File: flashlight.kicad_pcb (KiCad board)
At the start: 2 copper layers, 45 x 120 mm, 25 parts, among them J1 USB_B_Micro, J2 Conn_01x03_Pin, Q1 HSS2333, Q2 HSS2333, SW1 SW_DIP_x01, U1 LP4054HB5F, U2 MT3608

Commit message: copper pour
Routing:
- net Net-(U2-IN): track 41.4 -> 30.9 mm
- net Net-(D5-A): track 9.55 -> 0.00 mm
- net VOUT: track 20.0 -> 14.3 mm
- net Net-(D4-K): track 27.2 -> 28.2 mm
- added copper zone on B.Cu, net Net-(D5-A)
- added copper zone on B.Cu, net Net-(U2-IN)
- added copper zone on B.Cu, net VOUT

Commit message: v2.2.2
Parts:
- D2: value RED -> CHARGING
- D3: value GREEN -> CHARGED
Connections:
- net +5V renamed Net-(D1-A)
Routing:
- net GND: track 2.40 -> 0.00 mm
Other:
- board text added: "locked"

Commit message: tight sot23-6
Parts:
- removed R11: 10k, Resistor_SMD:R_0603_1608Metric
- U2: footprint Package_TO_SOT_SMD:SOT-23-6 -> SparkFun-Semiconductor-Standard:SOT23-6-Tight
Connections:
- C3 pad 1: Net-(U2-IN) -> Net-(U2-EN)
- L1 pad 1: Net-(U2-IN) -> Net-(U2-EN)
- SW1 pad 2: Net-(U2-IN) -> Net-(U2-EN)
- U2 pad 5: Net-(U2-IN) -> Net-(U2-EN)
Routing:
- net Net-(U2-IN): track 30.9 -> 0.00 mm
- net Net-(U2-EN): track 2.46 -> 30.9 mm
- added copper zone on B.Cu, net Net-(U2-EN)
- removed copper zone on B.Cu, net Net-(U2-IN)

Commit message: v2.3
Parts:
- moved C4 3.18 mm to (109.0, 134.1)
- moved U2 1.69 mm to (106.0, 132.9)
- moved D5 1.56 mm to (112.4, 133.2)
- moved R6 1.22 mm to (105.3, 136.1)
- moved R7 1.20 mm to (107.0, 136.1)
- moved C3 0.97 mm to (103.1, 132.8), turned to 90 degrees
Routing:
- net /Vf=0.6V: track 4.40 -> 2.33 mm
- net VOUT: track 14.3 -> 13.6 mm
- added copper zone on B.Cu, net /Vf=0.6V
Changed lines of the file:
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@@
   (net 19 "Net-(D3-K)")
   (footprint "Resistor_SMD:R_0603_1608Metric" (layer "B.Cu")
-    (at 107.9246 136.8896 -90)
+    (at 106.9848 136.144 -90)
     (descr "Resistor SMD 0603 (1608 Metric), square (rectangular) end terminal, IPC_7351 nominal, (Body size source: IPC-SM-782 page 72, https://www.pcb-3d.com/wordpress/wp-content/uploads/ipc-sm-782a_amendment_1_and_2.pdf), generated with kicad-footprint-generator")
     (tags "resistor")
@@
   )
   (footprint "Capacitor_SMD:C_0805_2012Metric" (layer "B.Cu")
-    (at 103.5812 131.962)
+    (at 103.0732 132.7912 90)
     (descr "Capacitor SMD 0805 (2012 Metric), square (rectangular) end terminal, IPC_7351 nominal, (Body size source: IPC-SM-782 page 76, https://www.pcb-3d.com/wordpress/wp-content/uploads/ipc-sm-782a_amendment_1_and_2.pdf, https://docs.google.com/spreadsheets/d/1BsfQQcO9C6DZCsRaXUlFlo91Tg2WpOkGARC1WS5S8t0/edit?usp=sharing), generated with kicad-footprint-generator")
     (tags "capacitor")
@@
     (zone_connect 2)
     (attr smd)
-    (fp_text reference "C3" (at -0.9906 2.0484 -90) (layer "B.SilkS")
-        (effects (font (size 1 1) (thickness 0.15)) (justify mirror))
-    )
-    (fp_text value "22uF/25V" (at 0 -1.68) (layer "B.Fab")
-        (effects (font (size 1 1) (thickness 0.15)) (justify mirror))
-    )
-    (fp_text user "${REFERENCE}" (at 0 0) (layer "B.Fab")
+    (fp_text reference "C3" (at -2.5908 0.1016) (layer "B.SilkS")
+        (effects (font (size 1 1) (thickness 0.15)) (justify mirror))
+    )
+    (fp_text value "22uF/25V" (at 0 -1.68 90) (layer "B.Fab")
+        (effects (font (size 1 1) (thickness 0.15)) (justify mirror))
+    )
+    (fp_text user "${REFERENCE}" (at 0 0 90) (layer "B.Fab")
         (effects (font (size 0.5 0.5) (thickness 0.08)) (justify mirror))
     )
@@
     (fp_line (start 1 0.625) (end 1 -0.625)
       (stroke (width 0.1) (type solid)) (layer "B.Fab"))
-    (pad "1" smd roundrect (at -0.95 0) (size 1 1.45) (layers "B.Cu" "B.Paste" "B.Mask") (roundrect_rratio 0.25)
+    (pad "1" smd roundrect (at -0.95 0 90) (size 1 1.45) (layers "B.Cu" "B.Paste" "B.Mask") (roundrect_rratio 0.25)
       (net 17 "Net-(U2-EN)") (pintype "passive"))
-    (pad "2" smd roundrect (at 0.95 0) (size 1 1.45) (layers "B.Cu" "B.Paste" "B.Mask") (roundrect_rratio 0.25)
+    (pad "2" smd roundrect (at 0.95 0 90) (size 1 1.45) (layers "B.Cu" "B.Paste" "B.Mask") (roundrect_rratio 0.25)
       (net 2 "GND") (pintype "passive"))
     (model "${KICAD6_3DMODEL_DIR}/Capacitor_SMD.3dshapes/C_0805_2012Metric.wrl"
@@
   )
   (footprint "Resistor_SMD:R_0603_1608Metric" (layer "B.Cu")
-    (at 106.2482 136.8642 -90)
+    (at 105.2576 136.144 -90)
     (descr "Resistor SMD 0603 (1608 Metric), square (rectangular) end terminal, IPC_7351 nominal, (Body size source: IPC-SM-782 page 72, https://www.pcb-3d.com/wordpress/wp-content/uploads/ipc-sm-782a_amendment_1_and_2.pdf), generated with kicad-footprint-generator")
     (tags "resistor")
@@
   )
   (footprint "SparkFun-Semiconductor-Standard:SOT23-6-Tight" (layer "B.Cu")
-    (at 107.6108 133.4098 180)
+    (at 106.0196 132.853 180)
     (descr "Footprint for SOT-26 part DMP2240UDM")
     (property "LCSC" "C84817")
@@
     (clearance 0.2)
     (zone_connect 2)
-    (fp_text reference "U2" (at 0 2.05) (layer "B.SilkS")
+    (fp_text reference "U2" (at 0 1.9414) (layer "B.SilkS")
         (effects (font (size 0.5 0.5) (thickness 0.1) bold) (justify mirror))
     )
@@
   )
   (footprint "Capacitor_SMD:C_0805_2012Metric" (layer "B.Cu")
-    (at 109.855 137.1182 90)
+    (at 108.966 134.0612 90)
     (descr "Capacitor SMD 0805 (2012 Metric), square (rectangular) end terminal, IPC_7351 nominal, (Body size source: IPC-SM-782 page 76, https://www.pcb-3d.com/wordpress/wp-content/uploads/ipc-sm-782a_amendment_1_and_2.pdf, https://docs.google.com/spreadsheets/d/1BsfQQcO9C6DZCsRaXUlFlo91Tg2WpOkGARC1WS5S8t0/edit?usp=sharing), generated with kicad-footprint-generator")
     (tags "capacitor")
@@
   )
   (footprint "Diode_SMD:D_SMB" (layer "B.Cu")
-    (at 113.284 134.502 90)
+    (at 112.4204 133.1976 90)
     (descr "Diode SMB (DO-214AA)")
     (tags "Diode SMB (DO-214AA)")
@@
   (segment (start 105.3186 51.0328) (end 107.7722 53.4864) (width 0.3) (layer "B.Cu") (net 4))
   (segment (start 104.6226 60.8494) (end 104.6226 68.7536) (width 1.2) (layer "B.Cu") (net 4))
-  (segment (start 98.425 147.066) (end 100.076 147.066) (width 0.8) (layer "B.Cu") (net 5))
-  (segment (start 100.076 147.066) (end 107.9246 139.2174) (width 0.8) (layer "B.Cu") (net 5))
-  (segment (start 107.9246 139.2174) (end 107.9246 137.7146) (width 0.8) (layer "B.Cu") (net 5))
+  (segment (start 106.9848 138.5062) (end 98.425 147.066) (width 0.8) (layer "B.Cu") (net 5))
+  (segment (start 106.9848 136.969) (end 106.9848 138.5062) (width 0.8) (layer "B.Cu") (net 5))
   (segment (start 84.582 50.195) (end 87.4312 50.195) (width 0.4) (layer "B.Cu") (net 6))
   (segment (start 89.14205 48.48415) (end 89.82795 48.48415) (width 0.4) (layer "B.Cu") (net 6))
@@
   (segment (start 105.2642 46.1537) (end 105.09 45.9795) (width 0.25) (layer "B.Cu") (net 15))
   (segment (start 107.6706 46.1537) (end 105.2642 46.1537) (width 0.25) (layer "B.Cu") (net 15))
-  (segment (start 106.3 137.6892) (end 107.9246 136.0646) (width 0.5) (layer "B.Cu") (net 16))
-  (segment (start 108.7483 134.9647) (end 108.7483 134.3598) (width 0.5) (layer "B.Cu") (net 16))
-  (segment (start 107.9246 136.0646) (end 107.9246 135.7884) (width 0.5) (layer "B.Cu") (net 16))
-  (segment (start 107.9246 135.7884) (end 108.7483 134.9647) (width 0.5) (layer "B.Cu") (net 16))
-  (segment (start 106.2482 137.6892) (end 106.3 137.6892) (width 0.5) (layer "B.Cu") (net 16))
+  (segment (start 105.3348 136.969) (end 106.9848 135.319) (width 0.5) (layer "B.Cu") (net 16))
   (segment (start 103.9434 104.3916) (end 103.9434 127.2122) (width 1.2) (layer "B.Cu") (net 17))
   (segment (start 109.656 98.679) (end 103.9434 104.3916) (width 1.2) (layer "B.Cu") (net 17))
   (segment (start 93.9706 52.8574) (end 93.996 52.832) (width 0.3) (layer "B.Cu") (net 19))
   (segment (start 91.4909 52.8574) (end 93.9706 52.8574) (width 0.3) (layer "B.Cu") (net 19))
-  (zone (net 9) (net_name "Net-(D5-A)") (layer "B.Cu") (hatch edge 0.5)
-    (priority 2)
-    (connect_pads yes (clearance 0.2))
-    (min_thickness 0.2) (filled_areas_thickness no)
-    (fill yes (thermal_gap 0.3) (thermal_bridge_width 0.3) (island_removal_mode 1) (island_area_min 10))
+  (zone (net 16) (net_name "/Vf=0.6V") (layer "B.Cu") (hatch edge 0.5)
+    (priority 4)
+    (connect_pads (clearance 0.2))
+    (min_thickness 0.25) (filled_areas_thickness no)
+    (fill yes (thermal_gap 0.5) (thermal_bridge_width 0.5))
     (polygon
       (pts
-        (xy 106.7816 124.841)
-        (xy 110.1598 124.841)
-        (xy 110.1598 130.6322)
-        (xy 114.6556 130.6322)
-        (xy 114.6556 133.6548)
-        (xy 111.7854 133.6548)
-        (xy 111.7854 132.7404)
-        (xy 108.4072 132.7404)
-        (xy 108.4072 130.2512)
-        (xy 106.7816 130.2512)
+        (xy 106.7816 133.5024)
+        (xy 107.696 133.5024)
+        (xy 107.696 135.7884)
+        (xy 106.5276 135.7884)
+        (xy 106.5276 134.8232)
+        (xy 106.7816 134.8232)
       )
     )
   )
-  (zone (net 17) (net_name "Net-(U2-EN)") (layer "B.Cu") (hatch edge 0.5)
+  (zone (net 9) (net_name "Net-(D5-A)") (layer "B.Cu") (hatch edge 0.5)
     (priority 3)
-    (connect_pads (clearance 0.2))
-    (min_thickness 0.2) (filled_areas_thickness no)
-    (fill yes (thermal_gap 0.3) (thermal_bridge_width 0.3) (island_removal_mode 1) (island_area_min 10))
+    (connect_pads yes (clearance 0.2))
+    (min_thickness 0.25) (filled_areas_thickness no)
+    (fill yes (thermal_gap 0.5) (thermal_bridge_width 0.5))
     (polygon
       (pts
-        (xy 105.156 124.8664)
-        (xy 105.156 129.4638)
-        (xy 103.3018 129.4638)
-        (xy 103.3018 133.0452)
-        (xy 106.8324 133.0452)
-        (xy 106.8324 133.7564)
-        (xy 106.8324 134.6708)
-        (xy 103.7336 134.6708)
-        (xy 101.9556 134.6708)
-        (xy 101.981 124.8664)
+        (xy 106.7816 132.2324)
+        (xy 113.6396 132.2324)
+        (xy 113.6396 129.6924)
+        (xy 109.1184 129.6924)
+        (xy 109.1184 124.9172)
+        (xy 106.7816 124.9172)
+      )
+    )
+  )
+  (zone (net 17) (net_name "Net-(U2-EN)") (layer "B.Cu") (hatch edge 0.5)
+    (priority 2)
+    (connect_pads (clearance 0.2))
+    (min_thickness 0.25) (filled_areas_thickness no)
+    (fill yes (thermal_gap 0.5) (thermal_bridge_width 0.5))
+    (polygon
+      (pts
+        (xy 105.3592 134.2644)
+        (xy 105.3592 132.5372)
+        (xy 104.1908 132.5372)
+        (xy 104.1908 133.1976)
+        (xy 101.9048 133.1976)
+        (xy 101.9048 129.54)
+        (xy 105.1052 129.54)
+        (xy 105.1052 124.968)
+        (xy 100.7364 124.968)
+        (xy 100.7364 134.2644)
       )
     )
@@
   (zone (net 5) (net_name "VOUT") (layer "B.Cu") (hatch edge 0.5)
     (priority 1)
-    (connect_pads (clearance 0.3))
+    (connect_pads (clearance 0.2))
     (min_thickness 0.25) (filled_areas_thickness no)
-    (fill yes (thermal_gap 0.3) (thermal_bridge_width 0.3))
+    (fill yes (thermal_gap 0.5) (thermal_bridge_width 0.5))
     (polygon
       (pts
-        (xy 107.315 138.684)
-        (xy 114.6556 138.684)
-        (xy 114.6556 135.3058)
-        (xy 111.887 135.3312)
-        (xy 111.887 137.2108)
-        (xy 107.5182 137.2108)
-        (xy 107.315 137.414)
+        (xy 106.426 137.414)
+        (xy 113.6396 137.414)
+        (xy 113.6396 134.0612)
+        (xy 108.1532 134.0612)
+        (xy 108.1532 136.4996)
+        (xy 106.426 136.4996)
       )
     )

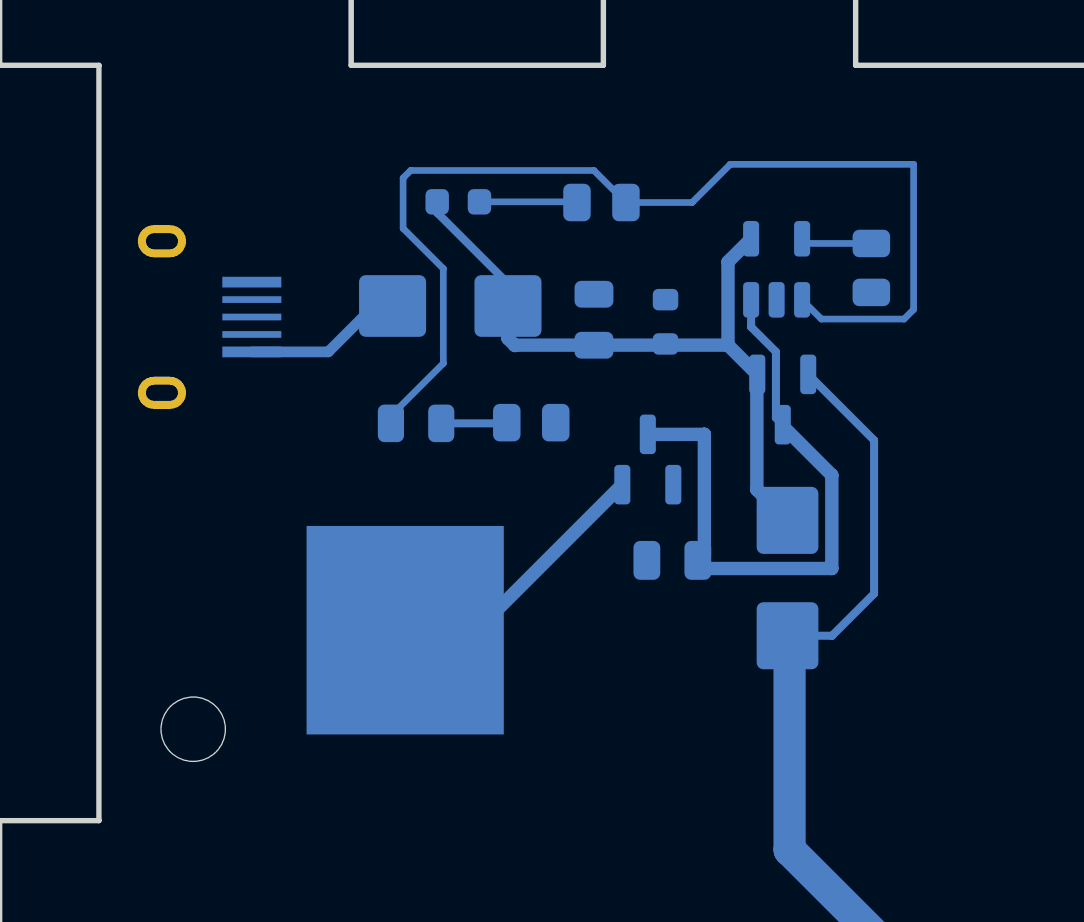
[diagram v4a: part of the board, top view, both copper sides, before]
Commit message: v2.4: double led
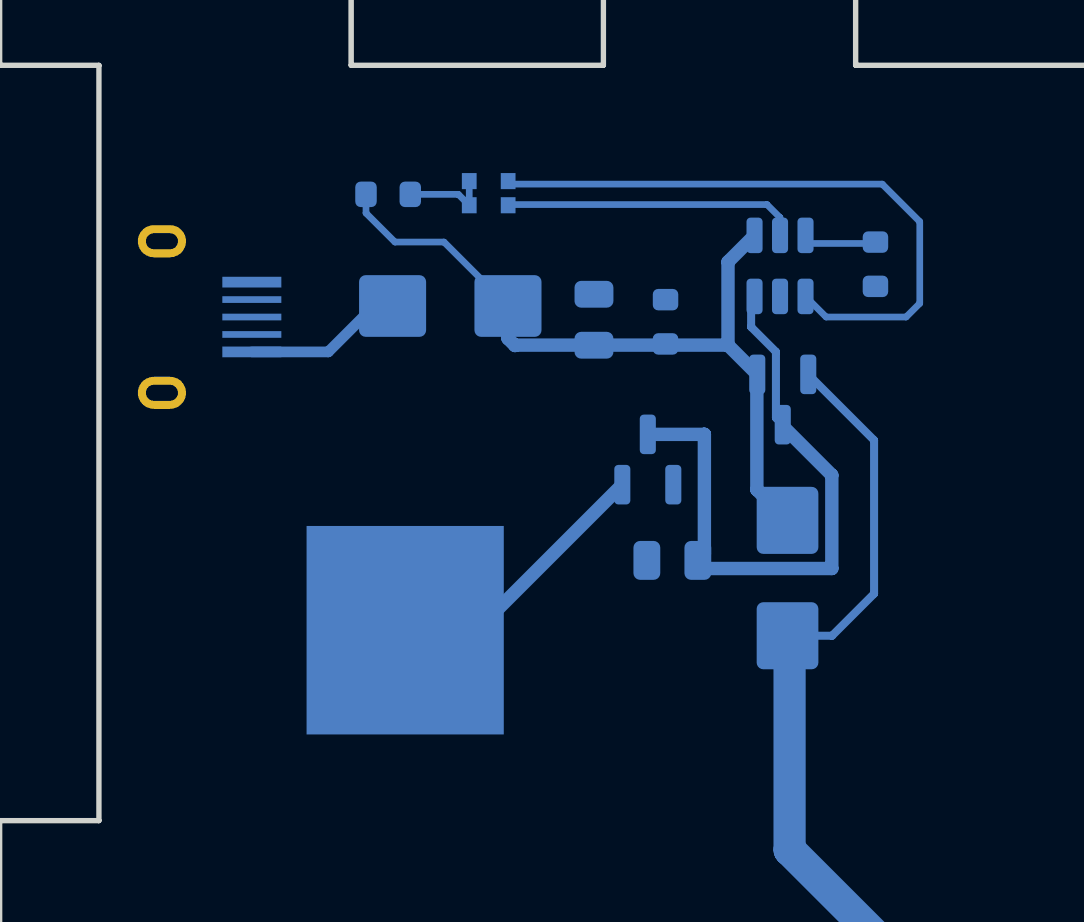
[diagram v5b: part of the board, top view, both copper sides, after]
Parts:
- removed D2: CHARGING, LED_SMD:LED_0603_1608Metric
- removed D3: CHARGED, LED_SMD:LED_0805_2012Metric
- removed R3: 1k, Resistor_SMD:R_0805_2012Metric
- removed U1: LP4054HB5F, Package_TO_SOT_SMD:SOT-23-5
- added U3: ~, Package_TO_SOT_SMD:SOT-23-6, B.Cu at (104.3, 47.0)
- added U4: ~, MyFootprints:R6BHC-A05_LED, B.Cu at (94.1, 43.8)
- BT1: footprint FlashlightLib:BH-18650 -> FlashlightLib:BH-18650_NoHole
- R1, R2: value 1k -> 2k2; footprint Resistor_SMD:R_0805_2012Metric -> Resistor_SMD:R_0603_1608Metric
- moved R2 7.96 mm to (89.7, 44.3)
- moved R1 0.21 mm to (107.8, 46.9)
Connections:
- R2 pad 1: Net-(D2-K) -> Net-(D1-K)
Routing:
- net Net-(U4-Blue+): track 40.8 -> 3.27 mm
- net Net-(U3-CHRG): track 0.00 -> 23.8 mm
- net Net-(U3-STDBY): track 0.00 -> 11.0 mm
- net Net-(D2-K): track 3.64 -> 0.00 mm
- net Net-(D3-K): track 2.52 -> 0.00 mm
- net Net-(D1-K): track 26.3 -> 28.8 mm
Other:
- board text added: "V2.3"
- board text removed: "locked"

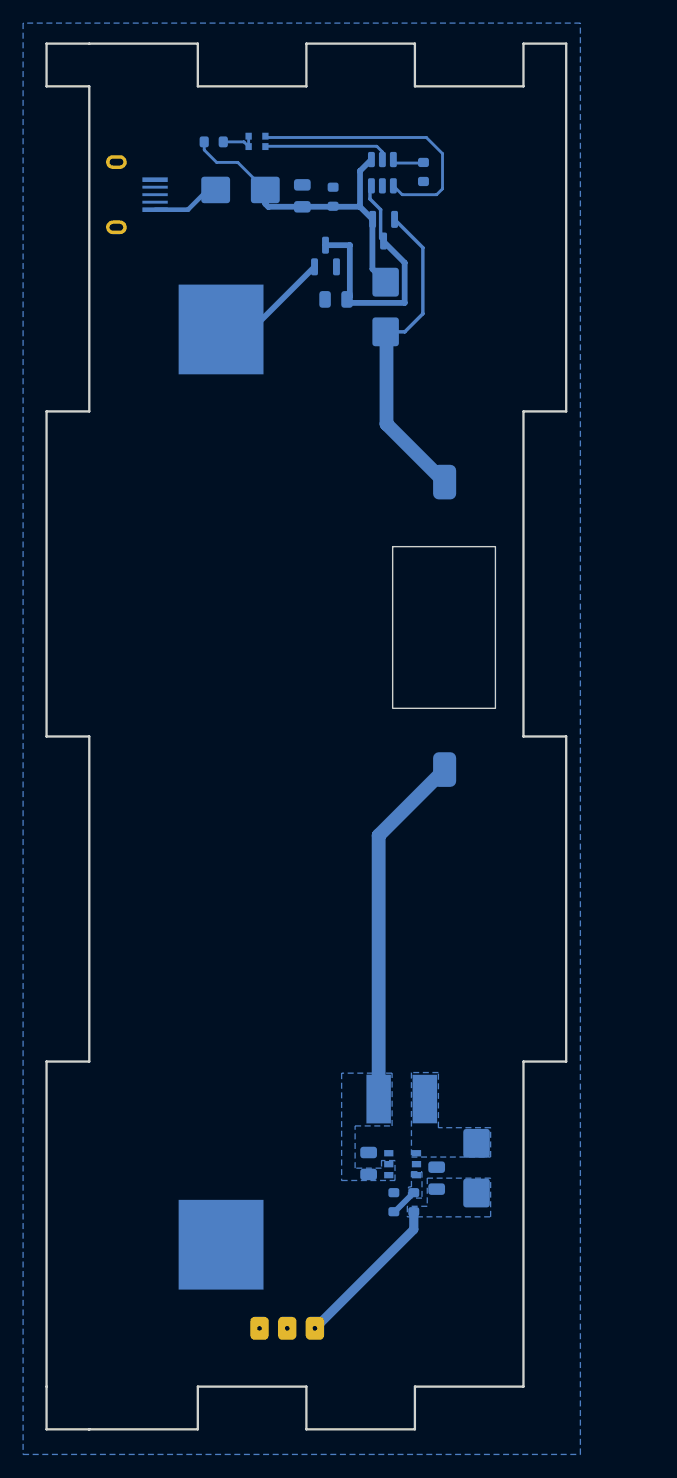
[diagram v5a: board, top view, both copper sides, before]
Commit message: v2.4 xb4908A undervoltage protection
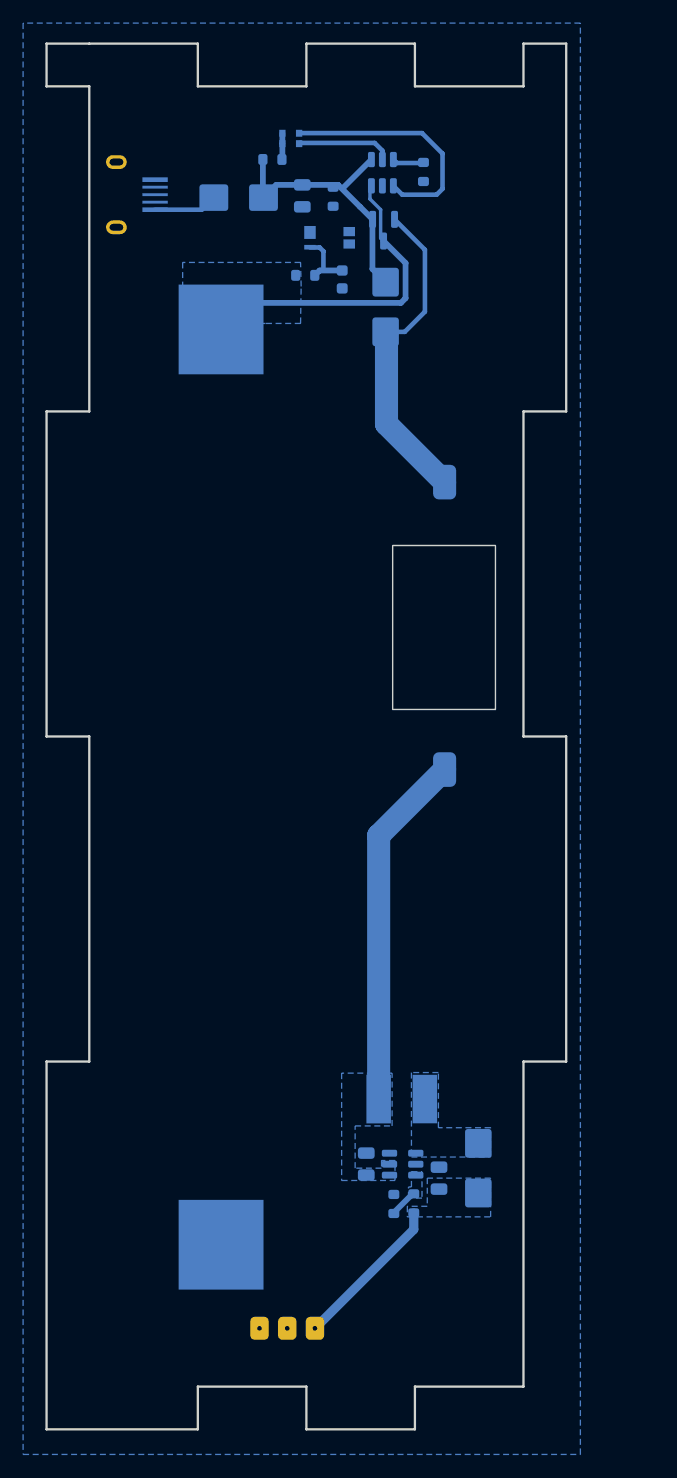
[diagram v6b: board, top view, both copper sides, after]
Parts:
- removed Q1: HSS2333, Package_TO_SOT_SMD:SOT-23
- added R3: 1k, Resistor_SMD:R_0603_1608Metric, B.Cu at (97.6, 55.9)
- added U1: XB4908A, FlashlightLib:XB4908A, B.Cu at (98.0, 53.4)
- C2: value 22uF/25V -> 1uF; footprint Capacitor_SMD:C_0805_2012Metric -> Capacitor_SMD:C_0603_1608Metric
- R1, R2: value 2k2 -> 1k
- U2: footprint SparkFun-Semiconductor-Standard:SOT23-6-Tight -> Package_TO_SOT_SMD:SOT-23-6
- U3: value ~ -> TP4057; footprint Package_TO_SOT_SMD:SOT-23-6 -> Package_TO_SOT_SMD:TSOT-23-6
- U4: value ~ -> R6BHC-A05_LED-19-223
- moved R2 5.30 mm to (94.7, 45.8)
- moved U4 2.93 mm to (97.0, 43.6)
- moved C2 1.81 mm to (100.8, 56.2), turned to -90 degrees
- moved D1 0.68 mm to (91.8, 49.1)
- moved C3 0.21 mm to (102.9, 132.8)
- moved C4 0.20 mm to (109.2, 134.1)
- moved D5 0.15 mm to (112.6, 133.2)
- moved R6 0.15 mm to (105.3, 136.3)
- moved R7 0.10 mm to (107.0, 136.2)
- turned C1 to -90 degrees
- turned R4 to -90 degrees
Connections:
- C2 pad 1: Net-(Q1-D) -> Net-(U1-VDD)
- Q2 pad 3: Net-(Q1-D) -> Net-(BT1-+)
- U3 pad 3: Net-(Q1-D) -> Net-(BT1-+)
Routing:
- net Net-(Q1-D): track 23.3 -> 0.00 mm
- net Net-(BT1-+): track 10.3 -> 28.0 mm
- net Net-(U1-VDD): track 0.00 -> 5.43 mm
- net Net-(D1-K): track 28.8 -> 23.9 mm
- net Net-(U3-~{CHRG}): track 23.8 -> 21.0 mm
- net Net-(U3-STDBY): track 11.0 -> 8.28 mm
- net Net-(U4-Blue+): track 3.27 -> 2.29 mm
- added copper zone on B.Cu, net Net-(BT1-+)
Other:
- outline, holes or cut-outs redrawn
- board text added: "V2.4"
- board text removed: "V2.3"
